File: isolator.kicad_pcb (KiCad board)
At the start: 4 copper layers, 120 x 75 mm, 125 parts, among them J1 HOST, J2 USB_C_Receptacle_PowerOnly_6P, J3 USB_A, J4 USB_A, J5 USB_C_Receptacle_USB2.0_16P, J6 USB_C_Receptacle_USB2.0_16P, Q1 2N7002, Q2 2N7002, T1 750313638, U1 ADuM4165, U10 TPS2553DBV, U11 TPS2553DBV, U12 TPS2553DBV, U13 TLV7041DBV, U14 TLV7041DBV, U15 USBLC6-2SC6, U16 USBLC6-2SC6, U17 USBLC6-2SC6, U18 USBLC6-2SC6, U2 USBLC6-2SC6, U3 USBLC6-2SC6, U4 USB2514B_Bi, U5 SN6505BDBV, U6 MIC29302WU, U7 TPS2121, U8 AP2112K-3.3, U9 TPS2553DBV, Y1 24M 8pF, Y2 24M 12pF

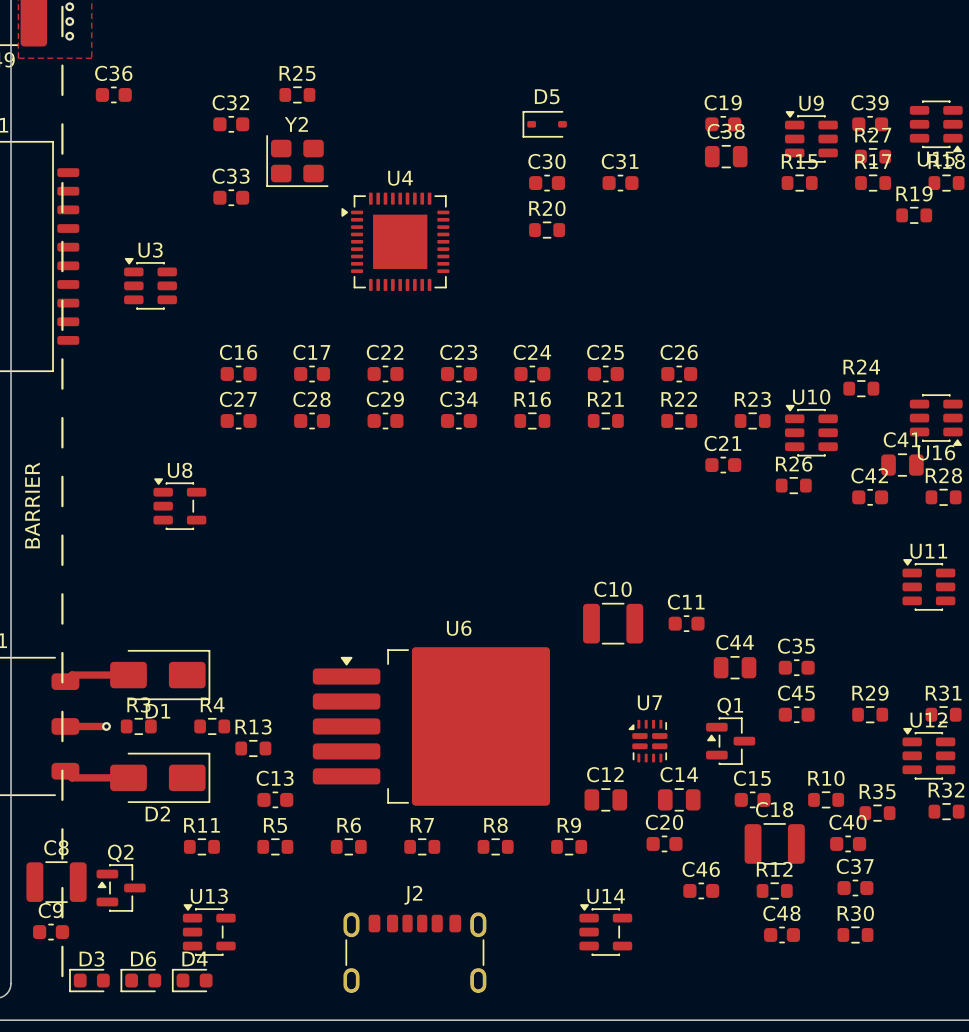
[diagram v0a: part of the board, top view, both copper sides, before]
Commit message: fix: decoupling audit fixes — tantalum C10 (T491D, polarity-correct), R36 330R min-load, 22u port bulk, re-seat ISO_5V bypass caps at their ICs per datasheet distances
Co-Authored-By: Claude Fable 5 <noreply@anthropic.com>
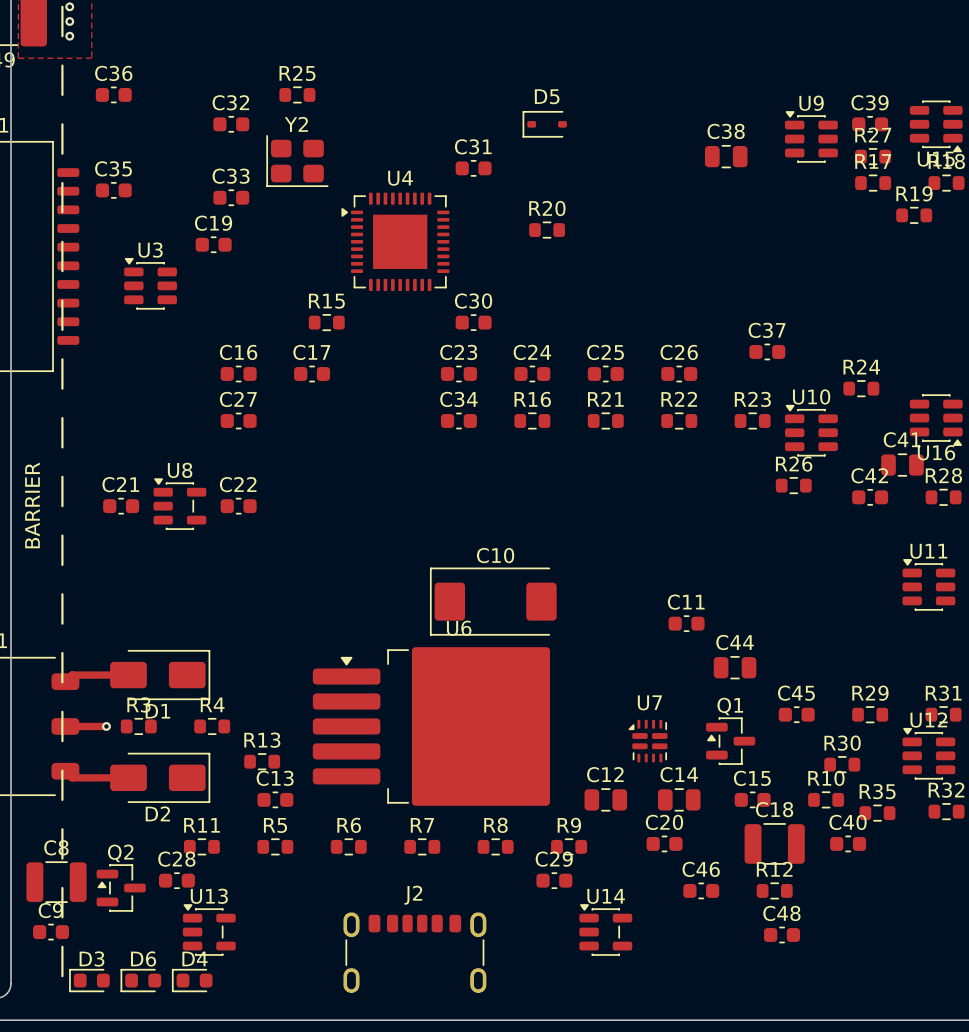
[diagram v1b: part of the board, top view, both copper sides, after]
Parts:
- C10: footprint Capacitor_SMD:C_1210_3225Metric -> CP_EIA-7343-31_Kemet-D
- C38, C41, C44, C47: value 10u -> 22u
- R36: value 1k -> 330R
- moved C35 56.7 mm to (96.5, 66.5)
- moved C21 41.1 mm to (97.0, 88.0)
- moved C37 37.0 mm to (141.0, 77.5)
- moved C19 35.7 mm to (103.3, 70.2)
- moved R15 33.6 mm to (111.0, 75.5)
- moved C29 33.3 mm to (126.5, 113.5)
- moved C28 32.6 mm to (100.8, 113.5)
- moved C22 13.5 mm to (105.0, 88.0)
- moved R30 11.6 mm to (146.1, 105.6)
- moved C30 10.7 mm to (121.0, 75.5)
- moved C31 10.0 mm to (121.0, 65.0)
- moved C10 8.14 mm to (122.5, 94.5)
- moved R13 1.08 mm to (106.6, 105.4)
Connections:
- C10 pad 1: GND2 -> /DCDC_5V
- C10 pad 2: /DCDC_5V -> GND2

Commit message: wip(pcb): zone refill
Co-Authored-By: Claude Fable 5 <noreply@anthropic.com>
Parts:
- added C10: 47u, Capacitor_Tantalum_SMD:CP_EIA-7343-31_Kemet-D, F.Cu at (99.6, 96.0)

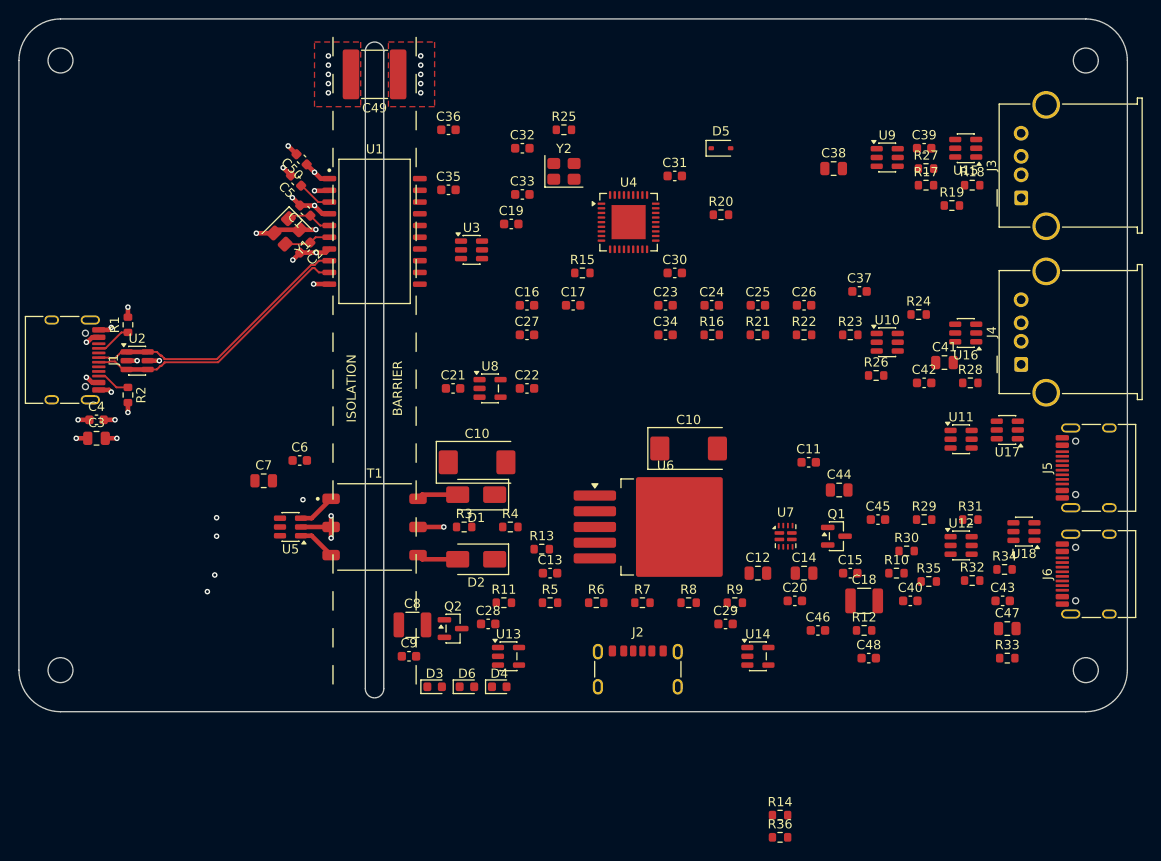
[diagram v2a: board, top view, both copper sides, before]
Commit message: feat(pcb): plane hookup pass — 94 stitching vias/stubs + QFN EP thermal vias, C10 dedupe (orphan removed, linked instance repositioned), crystal-area via fix
Co-Authored-By: Claude Fable 5 <noreply@anthropic.com>
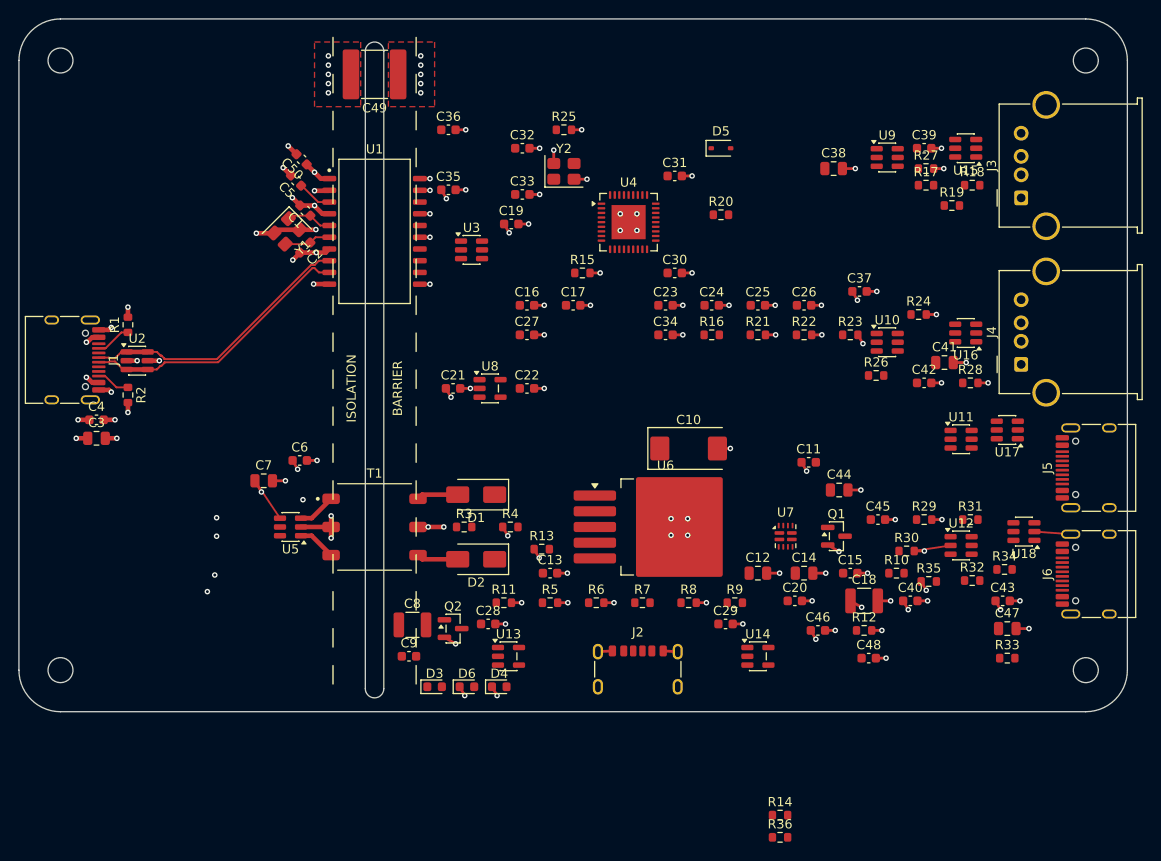
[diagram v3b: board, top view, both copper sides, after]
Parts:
- removed the C10 at (122.5, 94.5)
- moved C10 22.9 mm to (122.5, 94.5)
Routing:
- net GND2: track 2.80 -> 90.1 mm, vias 6 -> 80
- net /ISO_5V: track 0.00 -> 12.4 mm, vias 0 -> 11
- net GND1: track 30.2 -> 37.6 mm, vias 26 -> 28
- net /VBUS_HOST: track 15.6 -> 18.1 mm, vias 9 -> 11

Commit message: feat(pcb): route-ready passive placement — datasheet-oriented decoupling, chains, and port clusters
Co-Authored-By: Claude Fable 5 <noreply@anthropic.com>
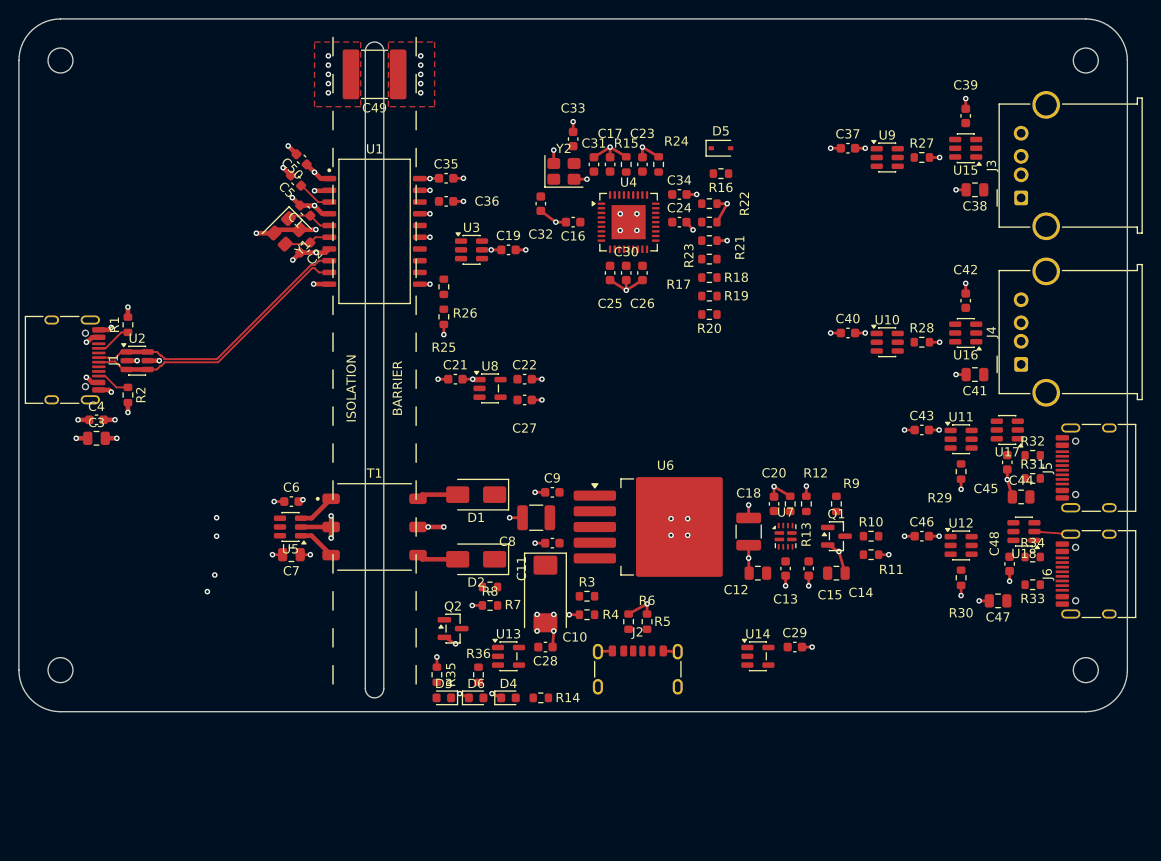
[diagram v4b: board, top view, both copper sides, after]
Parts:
- moved R35 54.2 mm to (95.2, 119.0), turned to -90 degrees
- moved R26 47.8 mm to (96.0, 77.0), turned to -90 degrees
- moved R11 40.1 mm to (142.2, 106.0)
- moved R36 37.1 mm to (99.8, 119.0), turned to -90 degrees
- moved R24 32.5 mm to (119.2, 63.8), turned to 90 degrees
- moved R18 30.2 mm to (124.8, 76.0)
- moved C40 29.8 mm to (139.8, 82.0), turned to 180 degrees
- moved C11 29.1 mm to (107.8, 104.8)
- moved R13 29.1 mm to (135.2, 100.5), turned to -90 degrees
- moved R14 28.8 mm to (106.5, 121.5), turned to 180 degrees
- moved R19 28.0 mm to (124.8, 78.0)
- moved C13 25.5 mm to (133.0, 107.5), turned to -90 degrees
- moved R17 24.8 mm to (124.8, 74.0)
- moved R25 24.1 mm to (96.0, 80.2), turned to -90 degrees
- moved C9 23.6 mm to (107.8, 99.2)
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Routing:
- net GND2: track 90.1 -> 97.8 mm, vias 80 -> 72
- net GND1: track 37.6 -> 32.4 mm
- net /VBUS_HOST: track 18.1 -> 17.2 mm, vias 11 -> 10
- net /ISO_5V: track 12.4 -> 12.3 mm, vias 11 -> 10

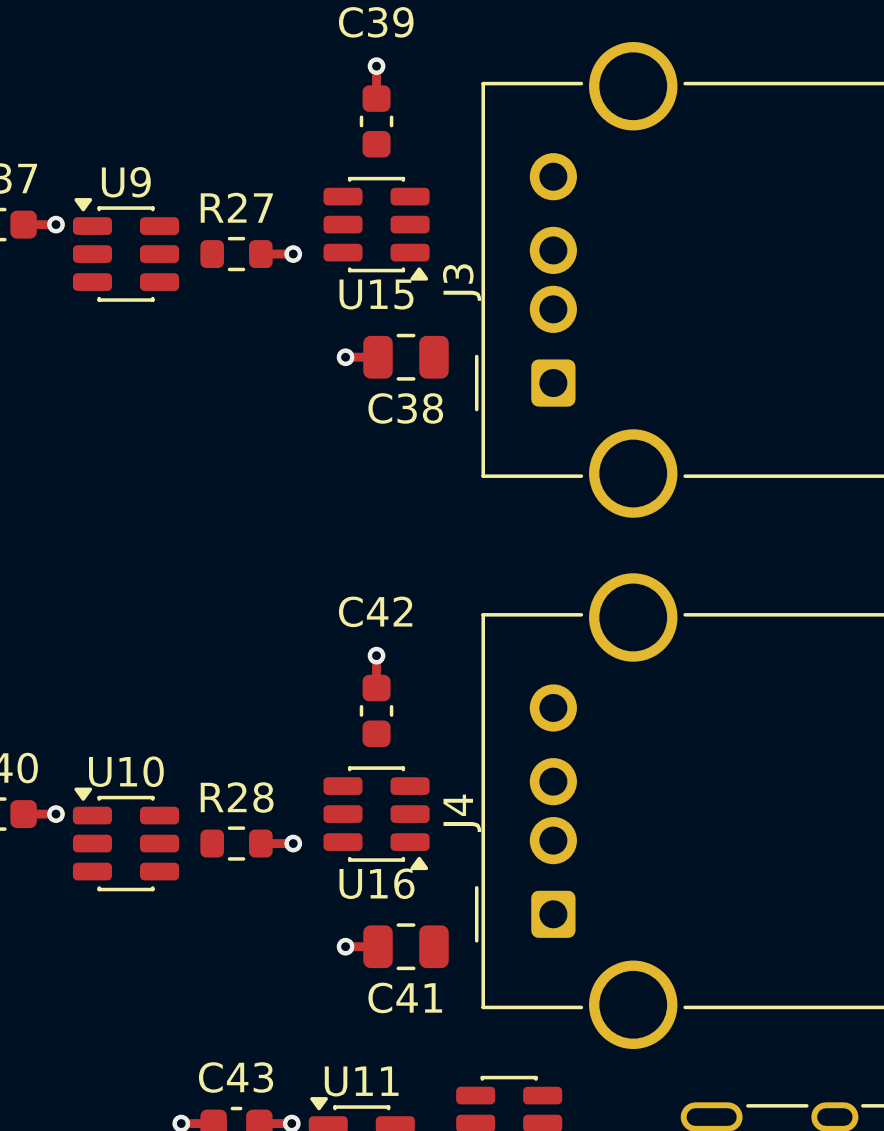
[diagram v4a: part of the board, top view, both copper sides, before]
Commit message: wip(pcb): user session — U15 realigned, port1 routing started
Co-Authored-By: Claude Fable 5 <noreply@anthropic.com>
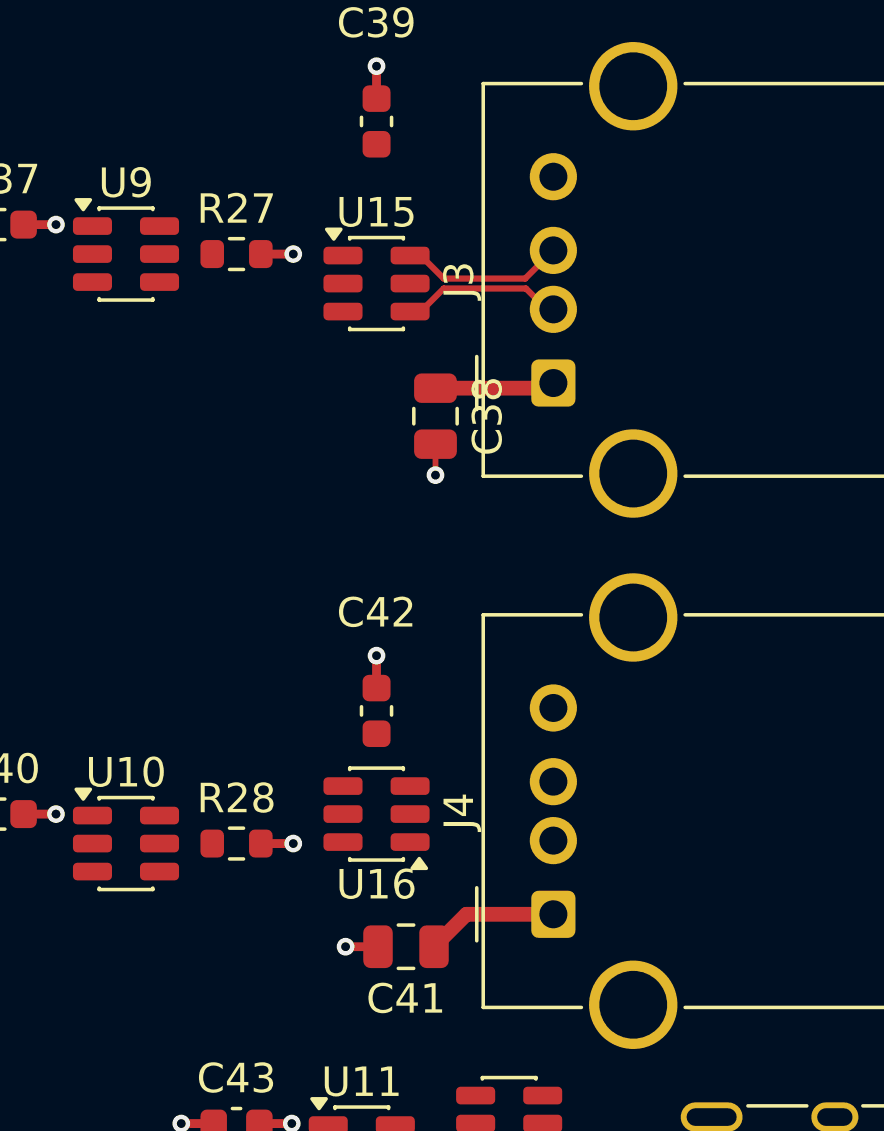
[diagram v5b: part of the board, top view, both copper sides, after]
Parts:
- moved C38 2.24 mm to (154.5, 68.5), turned to -90 degrees
- moved U15 2.00 mm to (152.5, 64.0), turned to 0 degrees
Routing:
- net /P1_D+: track 0.00 -> 5.58 mm
- net /P1_D-: track 0.00 -> 5.48 mm
- net /P2_VBUS: track 0.00 -> 4.51 mm
- net /P1_VBUS: track 0.00 -> 4.07 mm

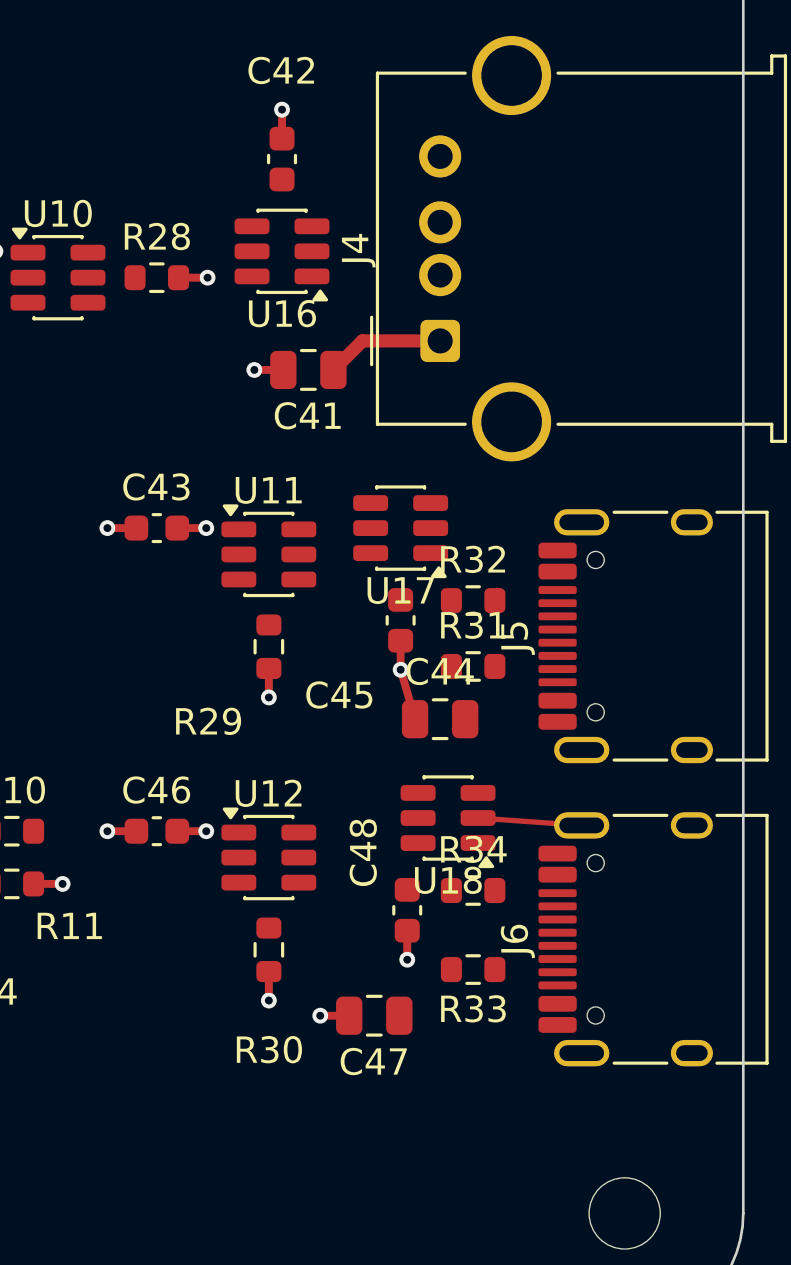
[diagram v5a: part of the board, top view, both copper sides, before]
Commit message: fix(pcb): USB ESD alignment — U16 derotated, U17/U18 centered on their connectors' D-pad axes; CC Rp/caps re-seated; stale fragments cleared
Co-Authored-By: Claude Fable 5 <noreply@anthropic.com>
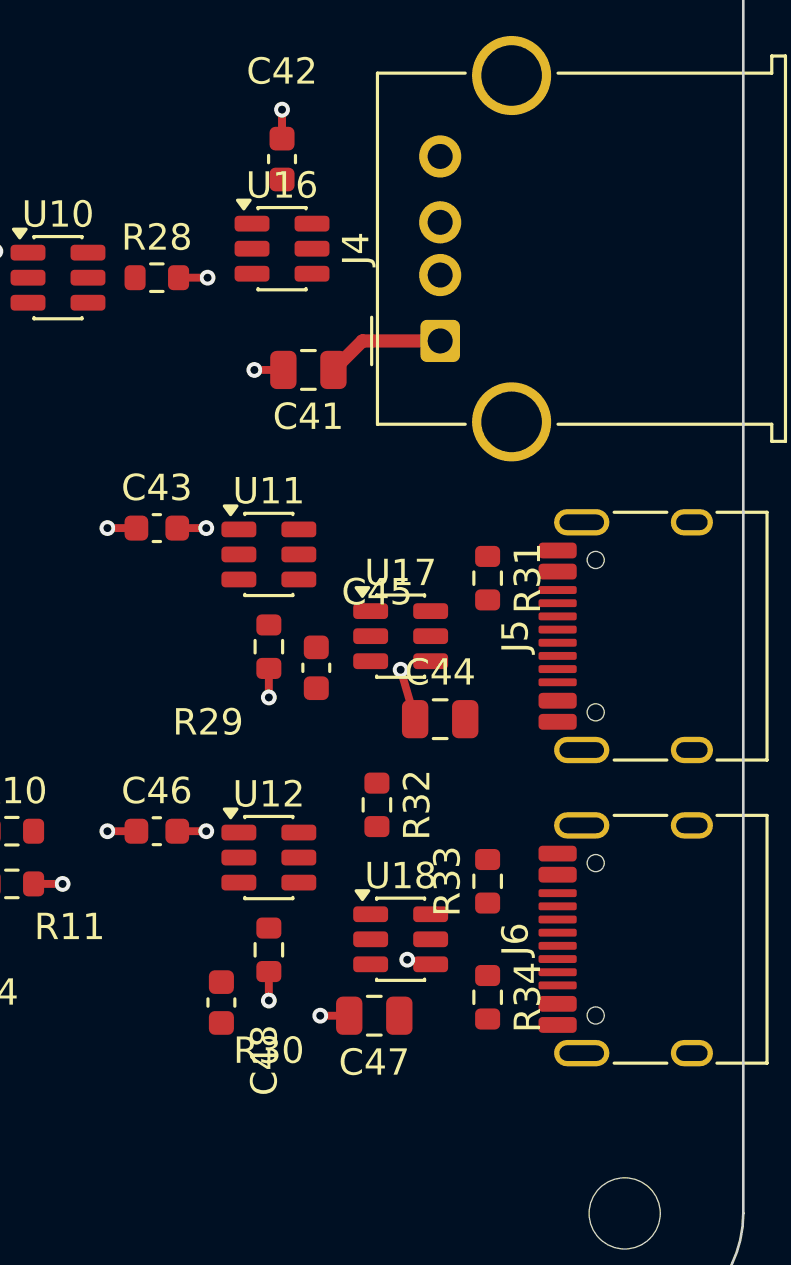
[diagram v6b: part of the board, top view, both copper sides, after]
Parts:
- moved R32 8.57 mm to (156.1, 103.0), turned to 90 degrees
- moved C48 7.87 mm to (150.2, 110.5), turned to 90 degrees
- moved U18 4.94 mm to (157.0, 108.1), turned to 0 degrees
- moved U17 4.10 mm to (157.0, 96.6), turned to 0 degrees
- moved R34 4.09 mm to (160.3, 110.3), turned to 90 degrees
- moved C45 3.67 mm to (153.8, 97.8), turned to 90 degrees
- moved R31 3.39 mm to (160.3, 94.4), turned to 90 degrees
- moved R33 3.39 mm to (160.3, 105.9), turned to 90 degrees
- moved U16 0.10 mm to (152.5, 81.9), turned to 0 degrees
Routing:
- net GND2: track 97.8 -> 91.6 mm, vias 72 -> 71
- net /P4_D-: vias 0 -> 1
